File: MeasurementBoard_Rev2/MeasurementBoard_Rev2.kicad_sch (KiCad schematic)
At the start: 5 parts

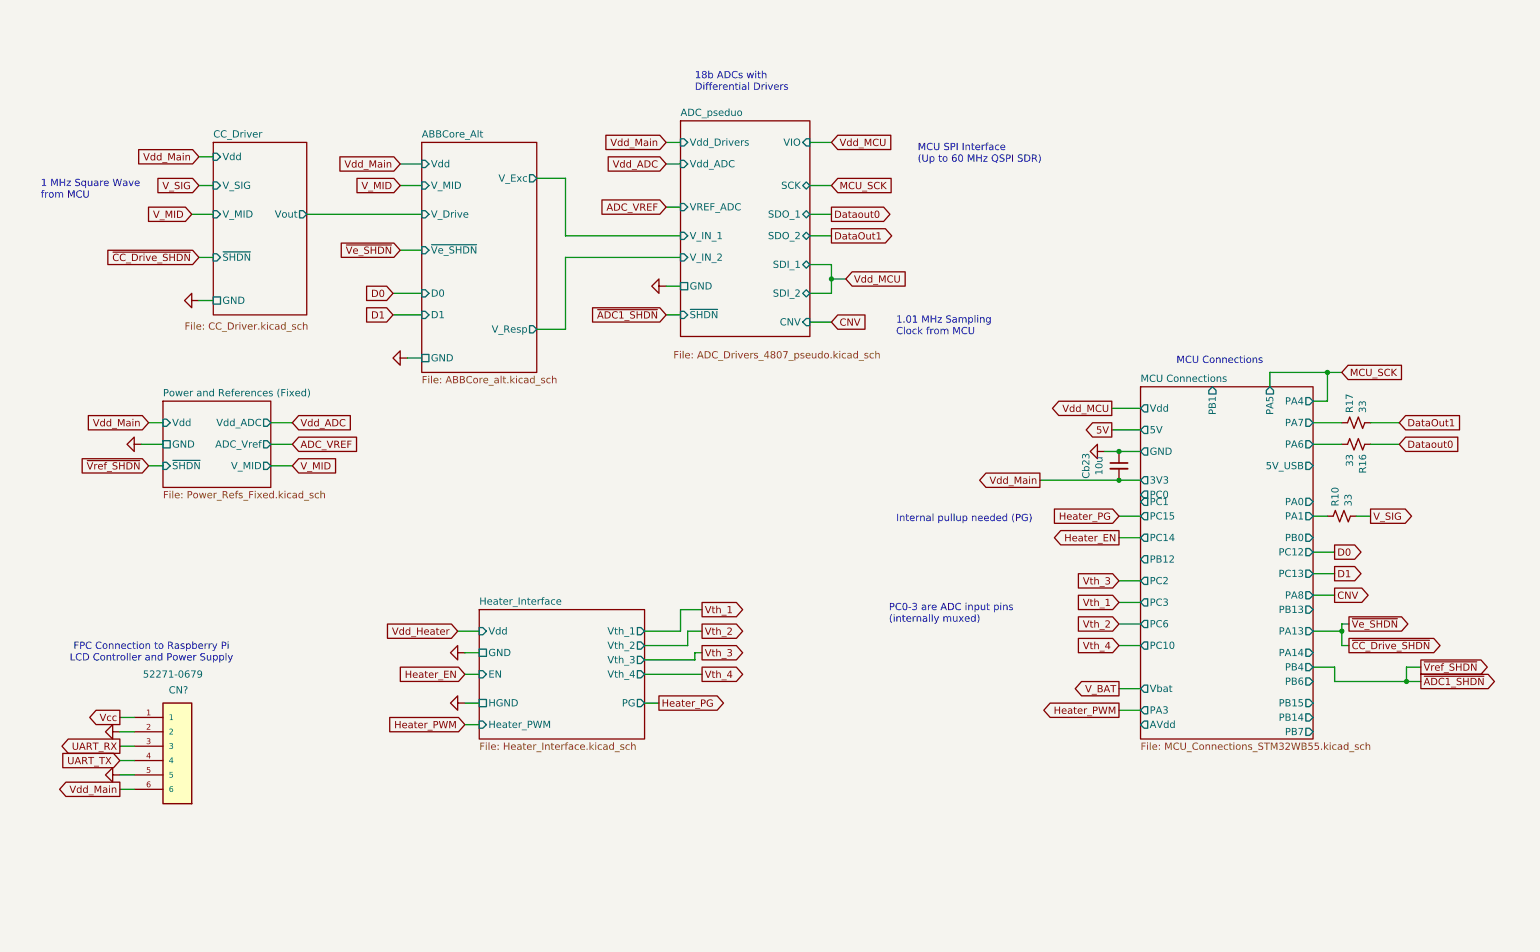
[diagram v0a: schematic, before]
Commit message: Finished Measurement Board Update Minus Heater Board Connections
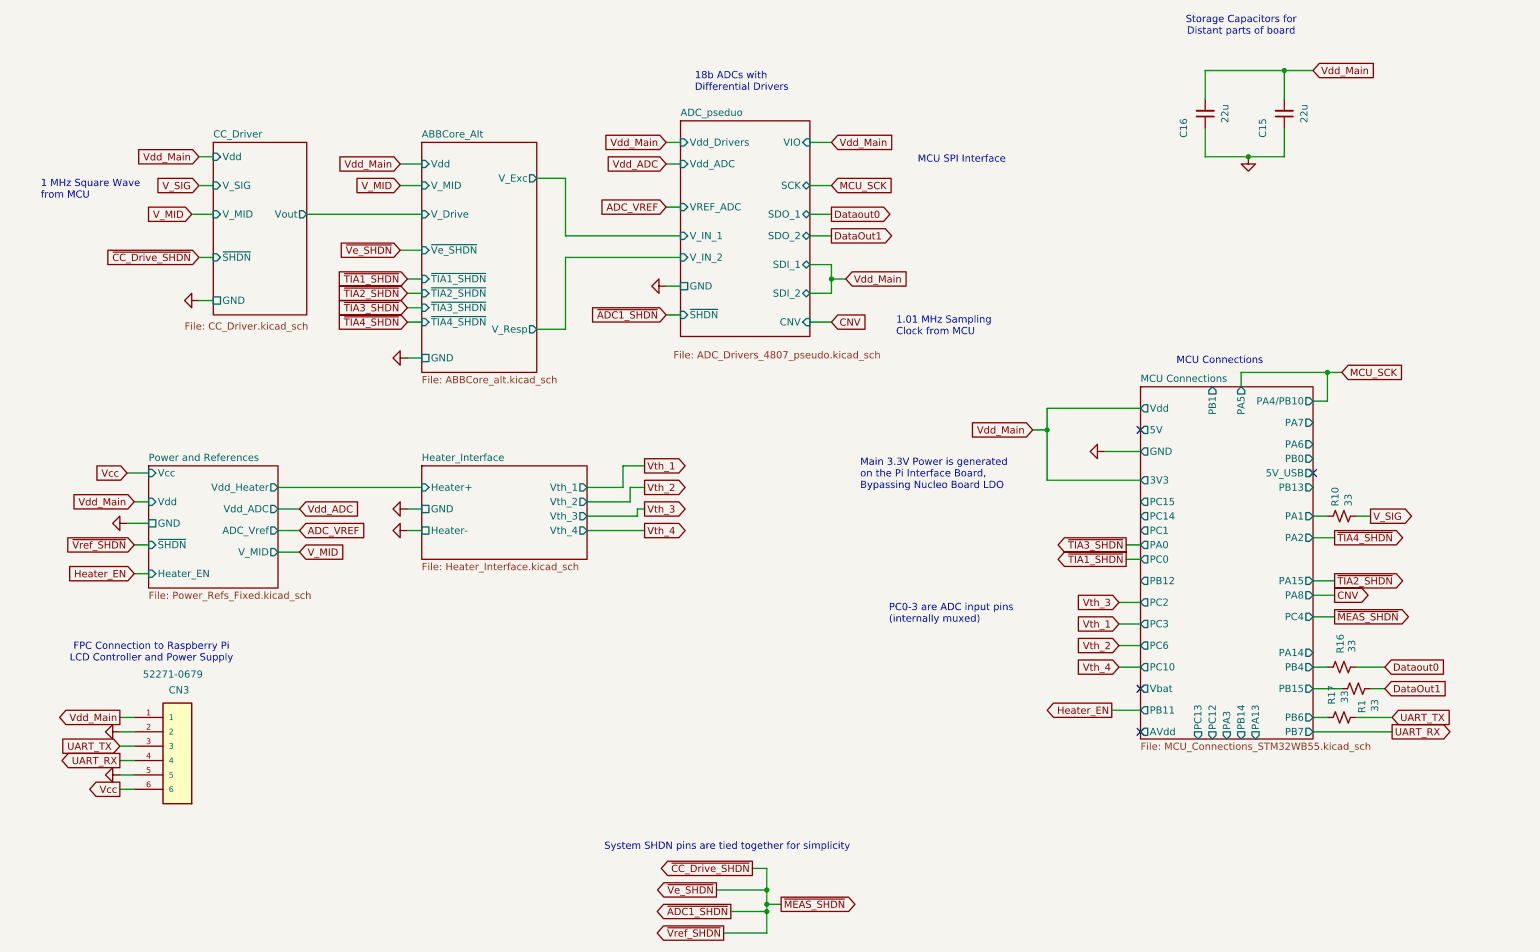
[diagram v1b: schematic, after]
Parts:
- removed Cb23: 10u, Capacitor_SMD:C_0603_1608Metric_Pad1.08x0.95mm_HandSolder, symbol Device:C_Small
- added C15, C16: 22u, Capacitor_SMD:C_0603_1608Metric_Pad1.08x0.95mm_HandSolder, symbol Device:C_Small
- added R1: 33, Resistor_SMD:R_0603_1608Metric_Pad0.98x0.95mm_HandSolder, symbol Device:R_Small_US
- CN3: renamed from CN?; footprint 52271-0679:MOLEX_52271-0679 -> GenIILibrary:MOLEX_52271-0679
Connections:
- net GND: now also C15.1, C16.1
- net MCU Connections/PA6: no longer R16.2
- net MCU Connections/PA7: no longer R17.1
- net MCU Connections/PB15: now also R17.1
- net MCU Connections/PB6: now also R1.1
- net UART_RX: now also CN3.4; no longer CN3.3
- net UART_TX: now also CN3.3, R1.2; no longer CN3.4
- net Vcc: now also CN3.6; no longer CN3.1
- net Vdd_Main: now also CN3.1, C15.2, C16.2; no longer CN3.6
- new net MCU Connections/PB4: R16.2
- no-connect marks 0 -> 4
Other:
- sheet Power and References (Fixed) renamed Power and References
- sheet ABBCore_Alt ports: added ~{TIA1_SHDN}, ~{TIA2_SHDN}, ~{TIA3_SHDN}, ~{TIA4_SHDN}; removed D0, D1
- sheet Heater_Interface ports: added Heater+, Heater-; removed EN, HGND, Heater_PWM, PG, Vdd
- sheet MCU Connections ports: added PA15, PA2, PA4/PB10, PB11, PC4; removed PA4
- sheet Power and References ports: added Heater_EN, Vcc, Vdd_Heater; removed none
- note added: "MCU SPI Interface"
- note added: "Main 3.3V Power is generated on the Pi Interface Board, Bypassing Nucleo Board LDO"
- note added: "Storage Capacitors for Distant parts of board"
- note added: "System SHDN pins are tied together for simplicity"
- note removed: "Internal pullup needed (PG)"
- note removed: "MCU SPI Interface (Up to 60 MHz QSPI SDR)"
- title: (none) -> Measurement Board
- moved on the sheet: R16, R17

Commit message: Nearly Finalized Boards
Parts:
- removed CN3: 52271-0679, GenIILibrary:MOLEX_52271-0679, symbol FrontEndPrototype_Rev1-rescue:52271-0679
- added CN3: 522070860, GenIILibrary:CON_522070860_MOL, symbol FrontEndPrototype_Rev1-rescue:522070860
- added R20, R21: 10k, Resistor_SMD:R_0603_1608Metric_Pad0.98x0.95mm_HandSolder, symbol Device:R_Small_US
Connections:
- net GND: now also CN3.4, CN3.7, R21.2
- net MCU Connections/PC1: now also R20.2, R21.1
- net UART_RX: now also CN3.5
- net UART_TX: now also CN3.6
- net Vcc: now also CN3.3
- net Vdd_Main: now also CN3.8
- new net V_Batt: CN3.1, R20.1
- new net ~{CHARGE_EN}: CN3.2
- no-connect marks 4 -> 6
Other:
- sheet Heater_Interface ports: added Vdd; removed Vth_3, Vth_4
- sheet MCU Connections ports: added PB2, PE4; removed none

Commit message: Final commit before order
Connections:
- net UART_RX: now also CN3.6; no longer CN3.5
- net UART_TX: now also CN3.5; no longer CN3.6

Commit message: Finished Measurement Board Fixes Schematic and PCB
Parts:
- added J9: Connector to Power Switch, Connector_PinHeader_2.54mm:PinHeader_1x04_P2.54mm_Vertical, symbol Connector:Conn_01x04_Pin
- added R22: 33, Resistor_SMD:R_0603_1608Metric_Pad0.98x0.95mm_HandSolder, symbol Device:R_Small_US
- added R23: 27k, Resistor_SMD:R_0603_1608Metric_Pad0.98x0.95mm_HandSolder, symbol Device:R_Small_US
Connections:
- net GND: now also CN3.2, CN3.5, J9.1 (Pin_1), J9.2 (Pin_2); no longer CN3.4, CN3.7
- net UART_RX: now also CN3.3; no longer CN3.6
- net UART_TX: now also CN3.4; no longer CN3.5
- net V_Batt: now also CN3.8; no longer CN3.1
- net Vcc: now also CN3.6; no longer CN3.3
- net Vdd_Main: now also J9.3 (Pin_3); no longer CN3.8
- net ~{CHARGE_EN}: now also CN3.7; no longer CN3.2
- new net Heater_PWM: R23.2
- new net MCU Connections/PB11: R22.2
- new net MCU Connections/PB8: R23.1
- new net ~{PWR_EN}: CN3.1, R22.1
- new net ~{Power_Switch_INT}: J9.4 (Pin_4)
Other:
- sheet MCU Connections ports: added PB8, PC5; removed none
- sheet Power and References ports: added 3V3, Heater_OUT, Heater_PWM; removed Heater_EN, Vdd_Heater
- moved on the sheet: CN3

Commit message: Final Rev3 Commit Post Submission
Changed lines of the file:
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@@
 	(wire
 		(pts
-			(xy 144.78 144.78) (xy 148.59 144.78)
-		)
-		(stroke
-			(width 0)
-			(type default)
-		)
-	)
-	(wire
-		(pts
 			(xy 220.98 44.45) (xy 220.98 49.53)
 		)
@@
 	(wire
 		(pts
-			(xy 139.7 146.05) (xy 144.78 146.05)
+			(xy 139.7 146.05) (xy 149.86 146.05)
 		)
 		(stroke
@@
 	(wire
 		(pts
-			(xy 144.78 146.05) (xy 144.78 144.78)
-		)
-		(stroke
-			(width 0)
-			(type default)
-		)
-	)
-	(wire
-		(pts
 			(xy 80.01 85.09) (xy 82.55 85.09)
 		)
@@
 	(global_label "~{Power_Switch_INT}"
 		(shape output)
-		(at 148.59 144.78 0)
+		(at 149.86 146.05 0)
 		(effects
 			(font
@@
 		)
 		(property "Intersheetrefs" "${INTERSHEET_REFS}"
-			(at 148.59 127 0)
+			(at 149.86 128.27 0)
 			(effects
 				(font
@@
 			)
 		)
-		(pin "Vdd" input
-			(at 34.29 110.49 180)
-			(effects
-				(font
-					(size 1.27 1.27)
-				)
-				(justify left)
-			)
-		)
 		(pin "Vdd_ADC" output
 			(at 57.15 111.76 0)
@@
 			)
 		)
+		(pin "Vdd" input
+			(at 34.29 110.49 180)
+			(effects
+				(font
+					(size 1.27 1.27)
+				)
+				(justify left)
+			)
+		)
